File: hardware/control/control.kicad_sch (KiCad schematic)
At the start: 66 parts, among them J1 Conn_01x05_Male, J2 DCDC-PWM, J3 display, J4 DCDC-MEASURES, J5 CANPWR, J6 CANGND, J7 RJ45, J8 RJ45, J9 Conn_02x03_Odd_Even, Q1 BSS123, SW1 next, SW2 select, U1 2.048V, U2 AP63200WU, U3 PIC18F27Q84, U4 TLE9250VSJXUMA1, Y1 10Mhz

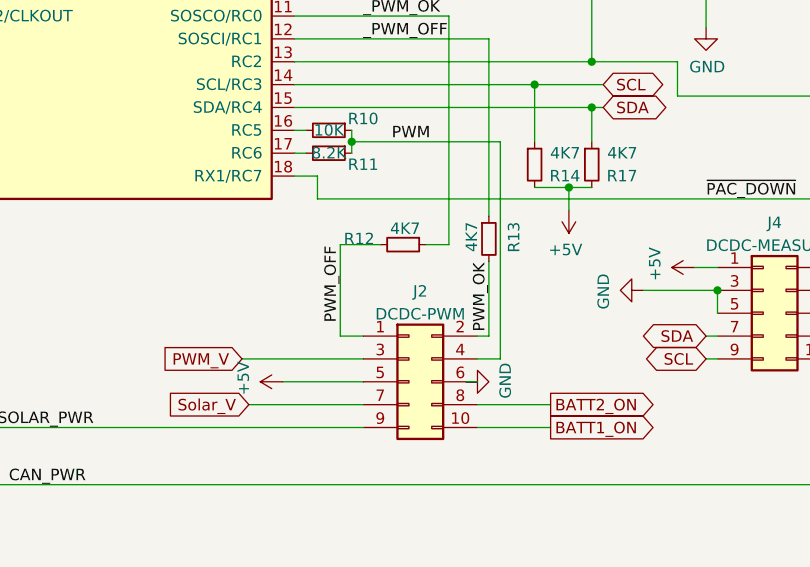
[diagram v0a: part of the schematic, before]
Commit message: Fix swapped signal names
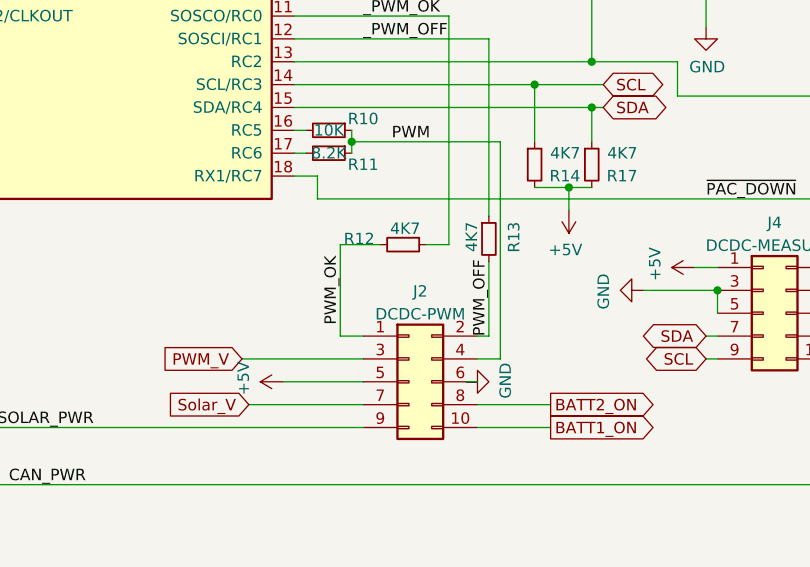
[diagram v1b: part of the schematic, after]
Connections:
- net PWM_OFF: now also J2.2 (Pin_2), R13.2; no longer J2.1 (Pin_1), R12.2
- net PWM_OK: now also J2.1 (Pin_1), R12.2; no longer J2.2 (Pin_2), R13.2
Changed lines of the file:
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@@
 	)
 	(label "PWM_OK"
-		(at 123.19 107.442 90)
+		(at 106.68 106.68 90)
 		(fields_autoplaced yes)
 		(effects
@@
 	)
 	(label "PWM_OFF"
-		(at 106.68 106.426 90)
+		(at 123.19 107.95 90)
 		(fields_autoplaced yes)
 		(effects
